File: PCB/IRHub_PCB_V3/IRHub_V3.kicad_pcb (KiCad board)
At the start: 2 copper layers, 79 x 79 mm, 97 parts, among them Q1 UMH3N, SW1 SW_Push, U1 DRV2605LDGS

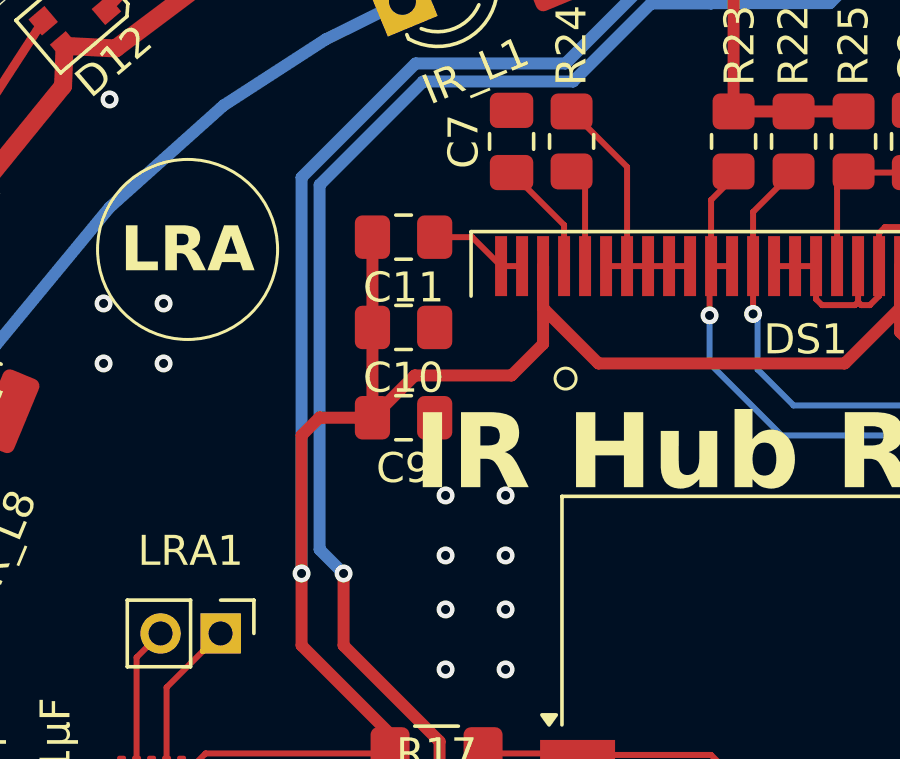
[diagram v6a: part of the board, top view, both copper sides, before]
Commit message: fix oled connector wiring
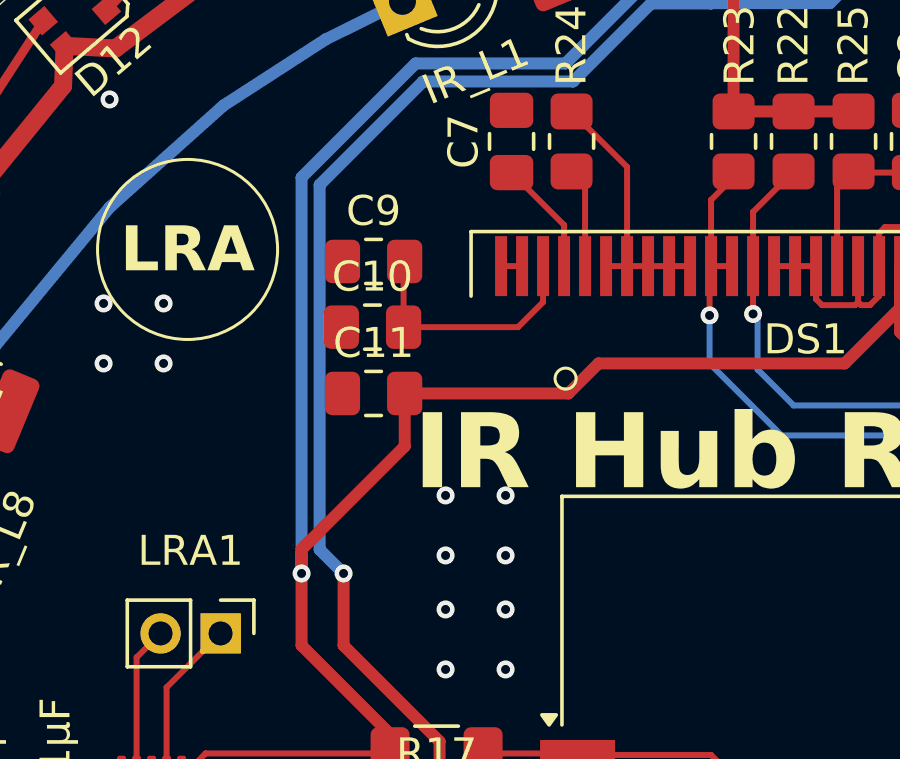
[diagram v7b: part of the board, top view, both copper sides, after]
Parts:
- C11: value 0.1µF -> 10µF
- moved C9 5.31 mm to (135.6, 79.6), turned to 0 degrees
- moved C11 5.31 mm to (135.6, 84.0), turned to 0 degrees
- moved C10 1.04 mm to (135.6, 81.8), turned to 0 degrees
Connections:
- C10 pad 2: +3.3V -> Net-(DS1-VCC)
- C9 pad 2: +3.3V -> Net-(DS1-VCC)
- DS1 pad 28: +3.3V -> Net-(DS1-VCC)
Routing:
- net +3.3V: track 263.2 -> 250.9 mm
- net Net-(DS1-VCC): track 0.00 -> 8.40 mm
- net GND: track 43.1 -> 40.5 mm
